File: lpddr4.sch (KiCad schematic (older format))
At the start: 23 parts, among them U1 MT53E256M16D1

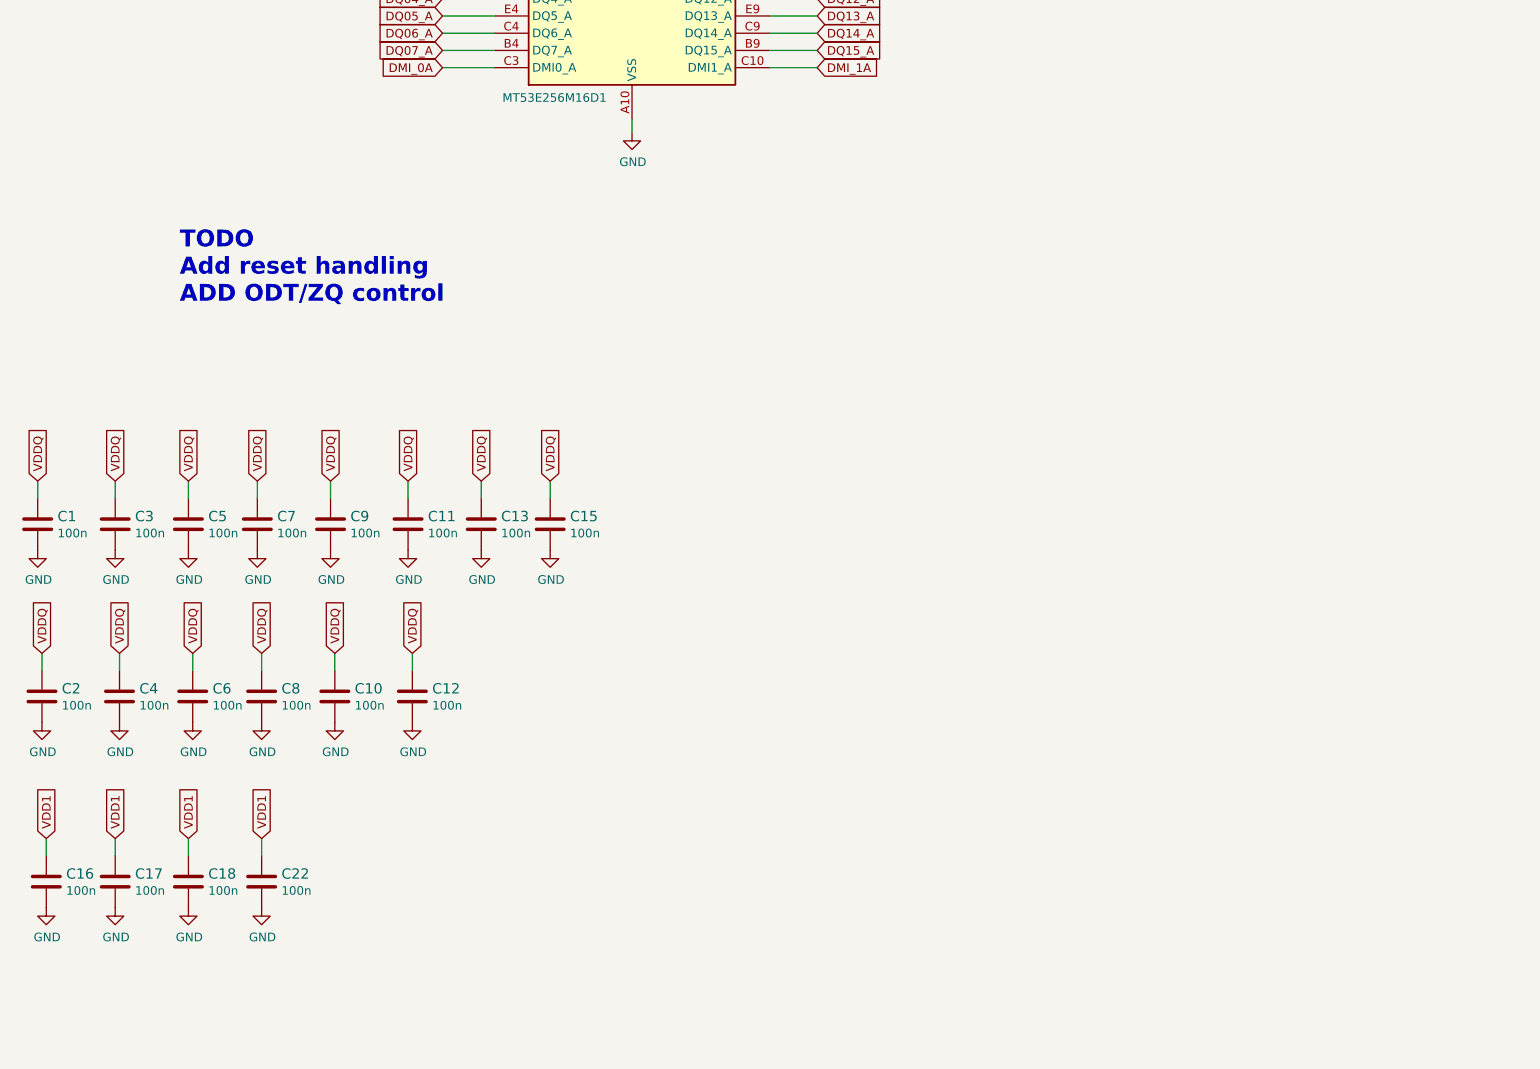
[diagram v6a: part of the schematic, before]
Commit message: Add filtering to VDD1
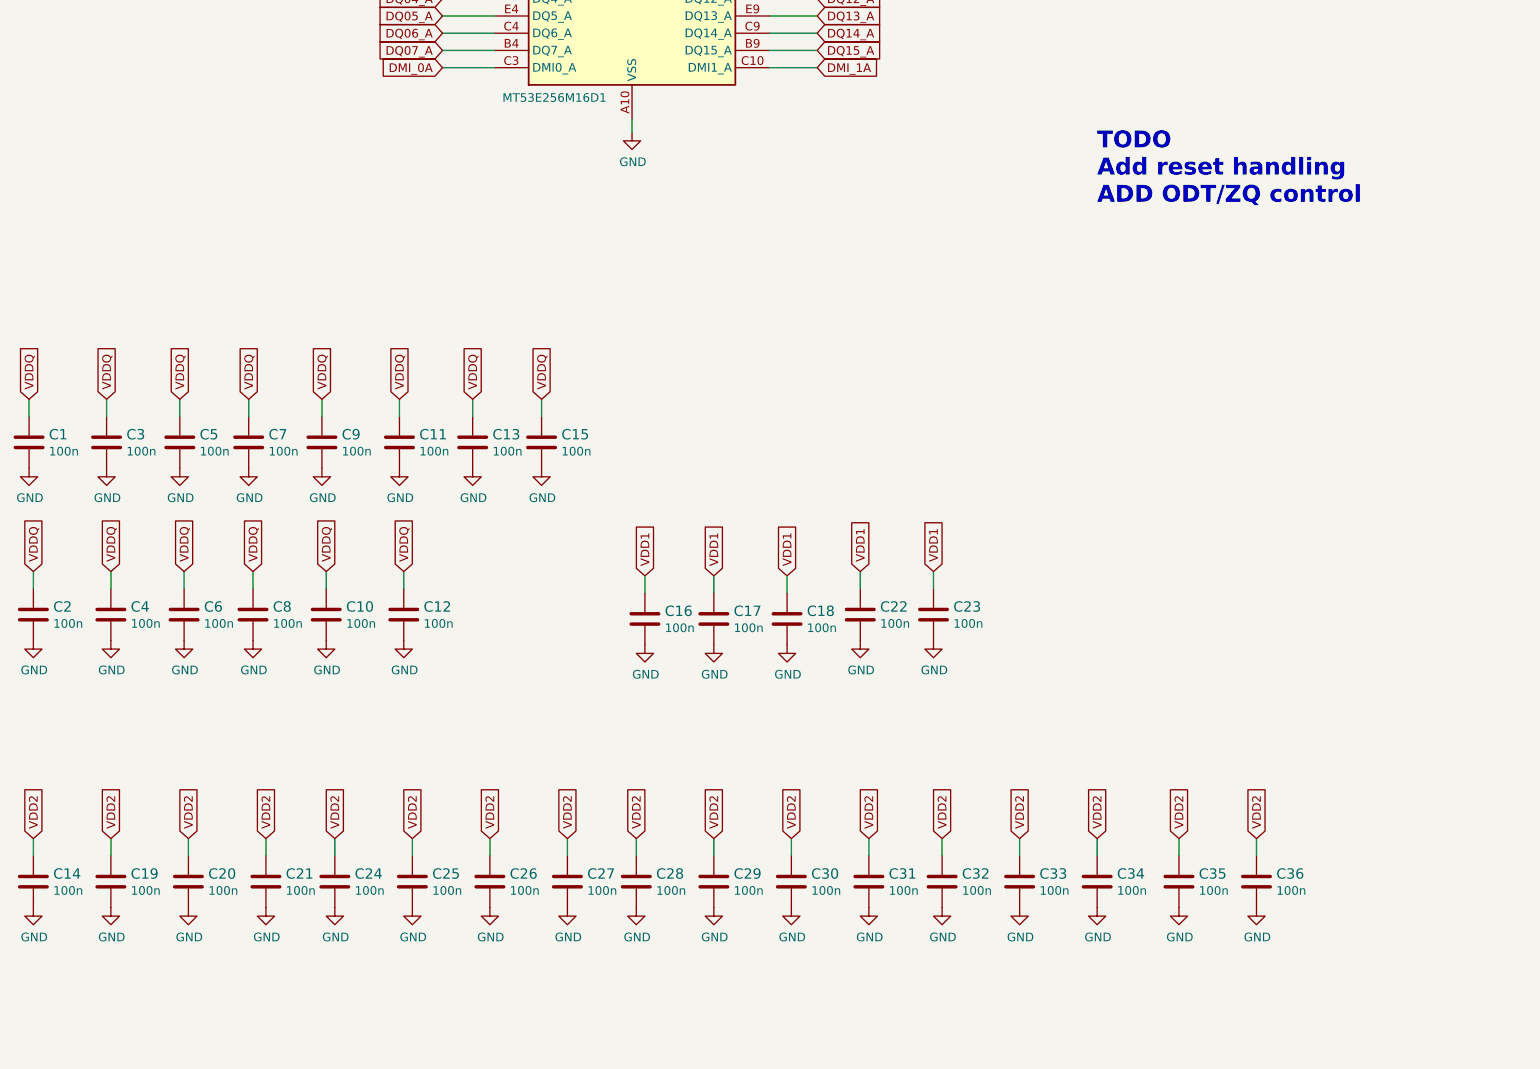
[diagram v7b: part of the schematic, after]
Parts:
- added C14, C19, C20, C21, C23, C24, C25, C26, C27, C28, C29, C30, C31, C32, C33, C34, C35, C36: C_100n_0201, antmicro-footprints:0201-res, symbol antmicroCapacitorsmisc:C_100n_0201
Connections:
- net GND: now also C14.2, C19.2, C20.2, C21.2, C23.2, C24.2, C25.2, C26.2, C27.2, C28.2, C29.2, C30.2, C31.2, C32.2, C33.2, C34.2, C35.2, C36.2
- net VDD1: now also C23.1
- net VDD2: now also C14.1, C19.1, C20.1, C21.1, C24.1, C25.1, C26.1, C27.1, C28.1, C29.1, C30.1, C31.1, C32.1, C33.1, C34.1, C35.1, C36.1
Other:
- moved on the sheet: C1, C10, C11, C12, C13, C15, C16, C17, C18, C2, C22, C3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

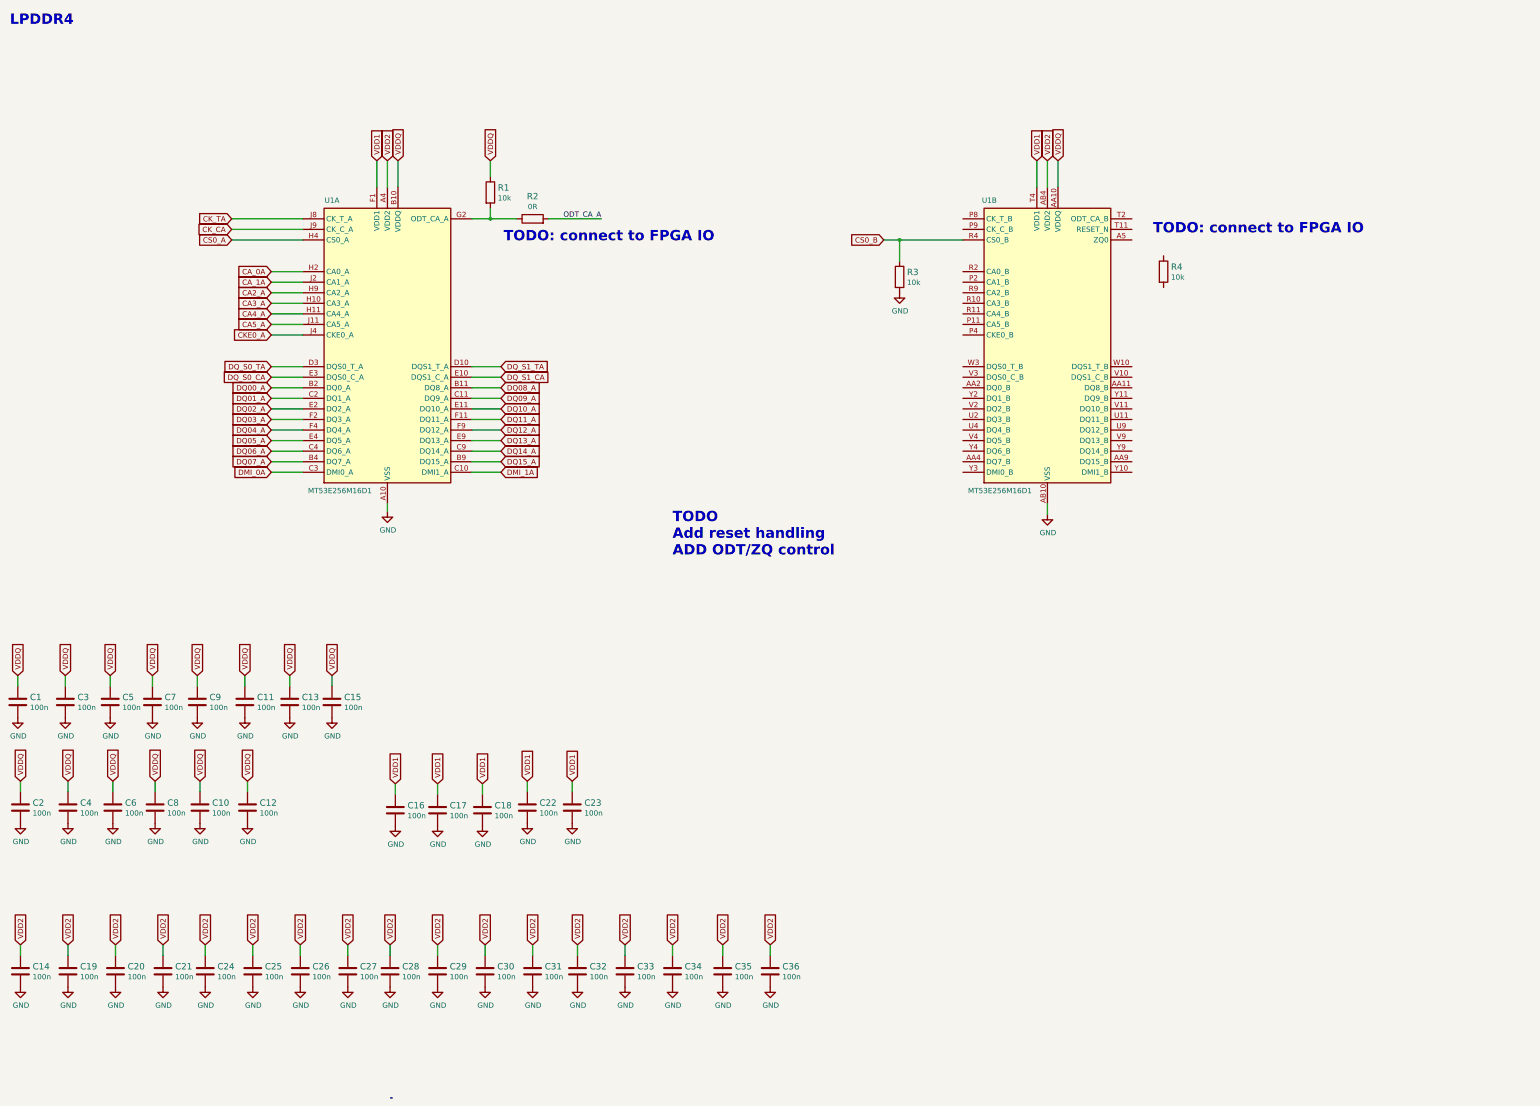
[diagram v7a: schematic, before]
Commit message: Fully routed, DRC clean
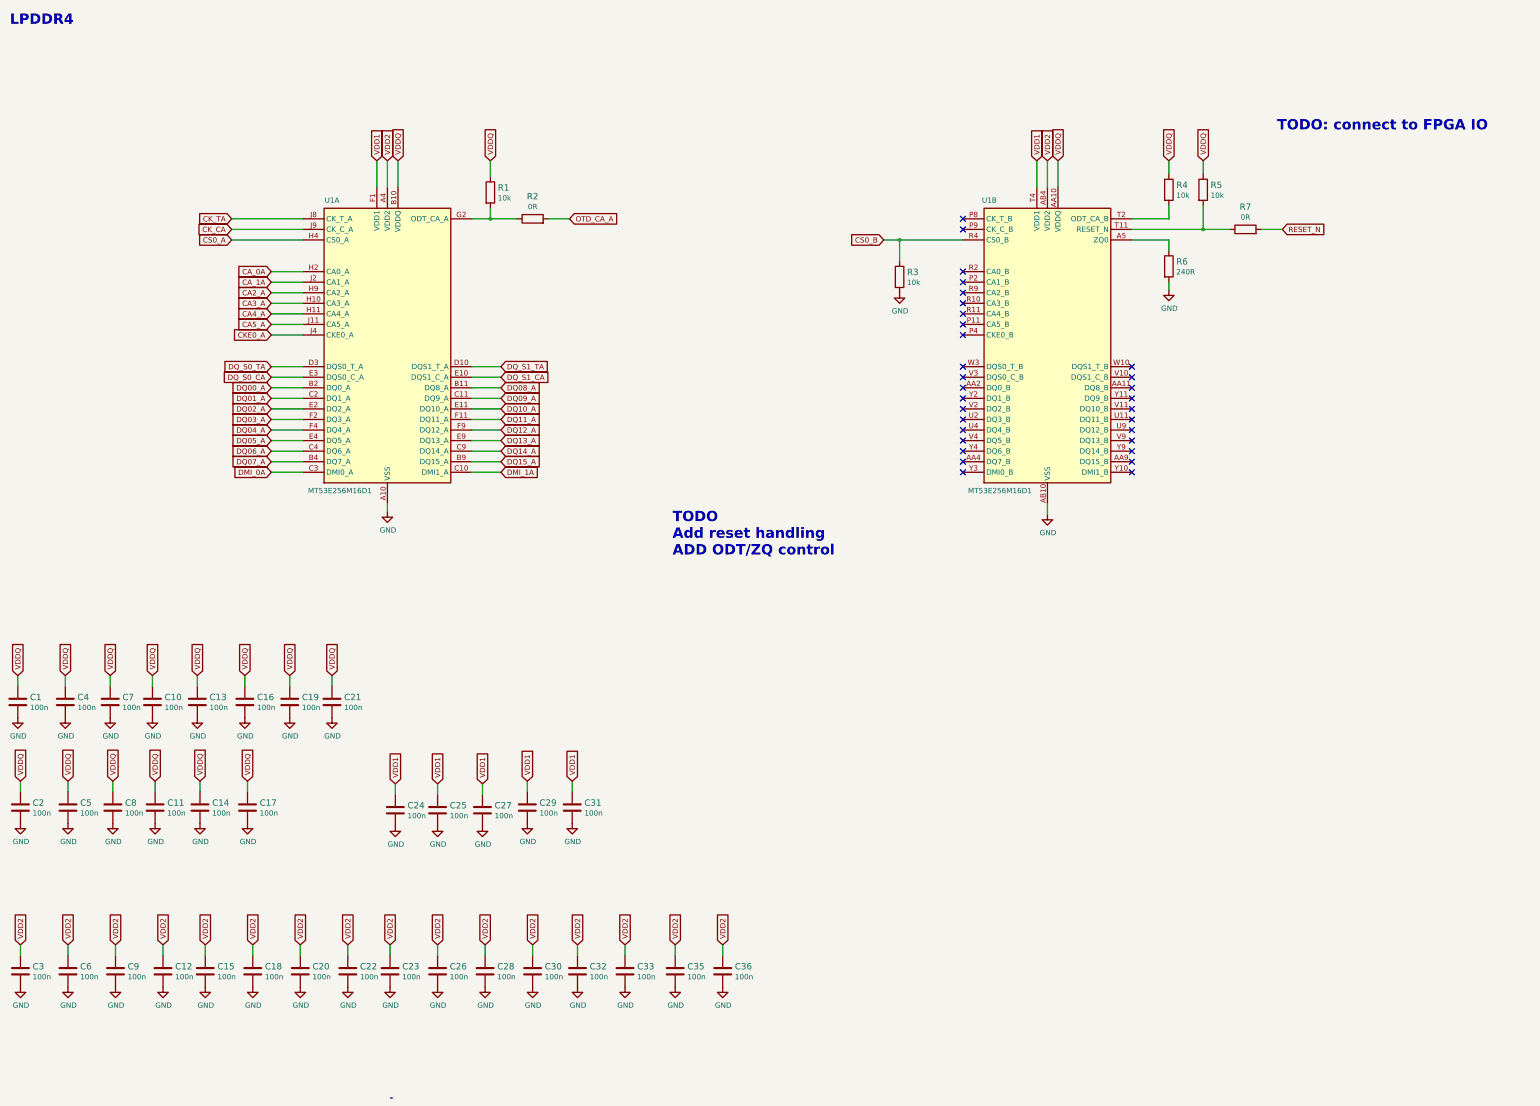
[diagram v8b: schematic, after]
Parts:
- removed C34: C_100n_0201, antmicro-footprints:0201-res, symbol antmicroCapacitorsmisc:C_100n_0201
- added R5: R_10k_0402, antmicro-footprints:0402-res, symbol antmicroResistors0402:R_10k_0402
- added R6: R_240R_0402, antmicro-footprints:0402-res, symbol antmicroResistors0402:R_240R_0402
- added R7: R_0R_0402, antmicro-footprints:0402-res, symbol antmicroResistors0402:R_0R_0402
- renumbered C7 to C10, C8 to C11, C21 to C12, C9 to C13, C10 to C14, C24 to C15, C11 to C16, C12 to C17, C25 to C18, C13 to C19, C26 to C20, C15 to C21, C27 to C22, C28 to C23, C16 to C24, C17 to C25, C29 to C26, C18 to C27, C30 to C28, C22 to C29, C14 to C3, C31 to C30, C23 to C31, C3 to C4, C4 to C5, C19 to C6, C5 to C7, C6 to C8, C20 to C9
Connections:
- net GND: now also R6.2
- net VDDQ: now also R4.1, R5.1
- net at R4.2: now also U1.T2 (ODT_CA_B)
- net at U1.A5 (ZQ0): now also R6.1
- net at U1.T11 (RESET_N): now also R5.2, R7.1
- net ODT_CA_A renamed OTD_CA_A
- new net RESET_N: R7.2
- no-connect marks 0 -> 31
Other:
- moved on the sheet: C35, C36
